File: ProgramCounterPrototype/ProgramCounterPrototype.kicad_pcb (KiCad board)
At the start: 4 copper layers, 68.6 x 45.7 mm, 13 parts, among them J1 Screw_Terminal_01x02, J2 Y, J5 Ctl, J6 PC, U1 ATF22V10C-7PX, U2 IDT7381

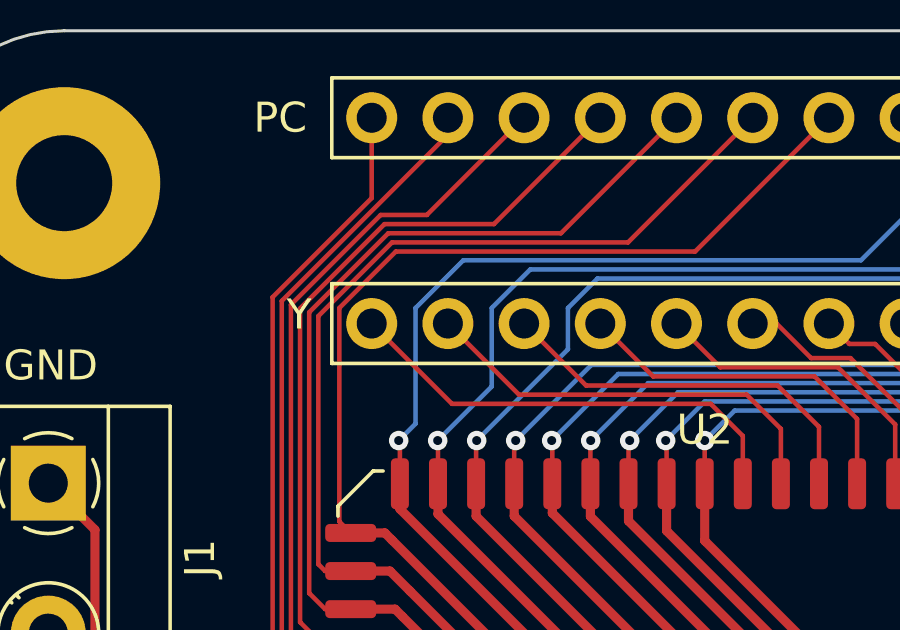
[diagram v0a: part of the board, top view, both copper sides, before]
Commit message: Add a version number to the Program Counter Prototype PCB
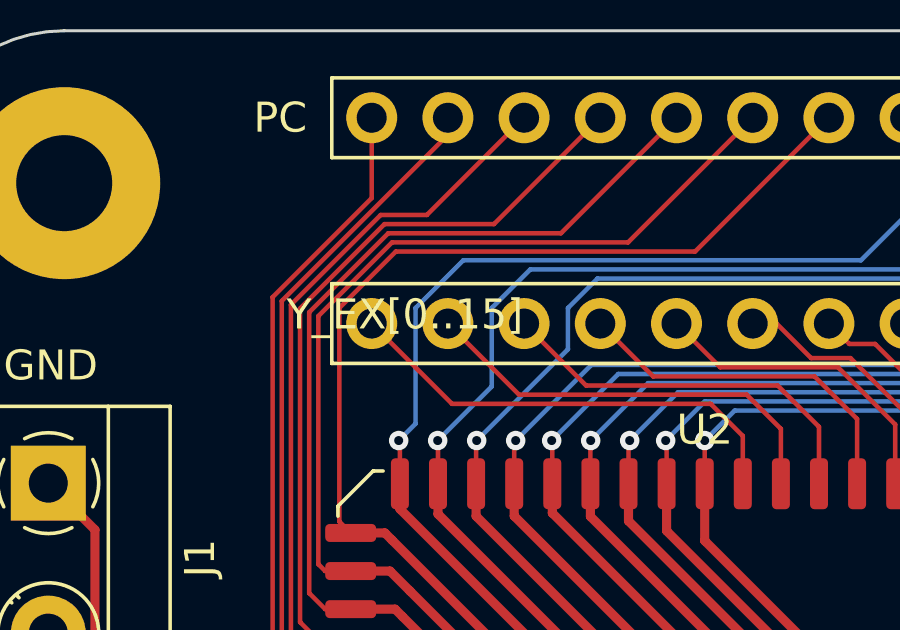
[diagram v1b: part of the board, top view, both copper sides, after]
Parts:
- J2: value Y -> Y_EX[0..15]

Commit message: Program Counter bypasses the A and B registers and uses F.
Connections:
- U2 pad 25: VCC -> GND
- U2 pad 26: VCC -> GND
- U2 pad 50: GND -> VCC
- U2 pad 51: GND -> VCC
- U2 pad 52: GND -> VCC
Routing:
- net VCC: track 22.0 -> 25.2 mm
- net GND: track 29.1 -> 25.9 mm

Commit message: Update version numbers in KiCAD again.
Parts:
- turned C1 to 180 degrees
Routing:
- net GND: track 25.9 -> 193.6 mm, vias 4 -> 0
- net VCC: track 25.2 -> 84.0 mm, vias 2 -> 1
- net Phi1b: track 66.8 -> 67.7 mm
- removed copper zone on In1.Cu, net GND
- removed copper zone on In2.Cu, net VCC
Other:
- copper layers 4 -> 2
- board text added: "Program Counter, Rev A (d86d9981) Copyright © 2021 Andrew Fox"
- board text removed: "Program Counter, Rev A (fd678fbe) Copyright © 2021 Andrew Fox"
